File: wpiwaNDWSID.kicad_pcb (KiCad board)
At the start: 2 copper layers, 25 parts, among them J1 Conn_01x06, J2 Conn_01x03, J3 Conn_01x03, J4 Conn_01x03, J5 Conn_01x02, J6 Conn_01x03, U1 ESP32-S3-WROOM-1, U2 74AHCT125, U3 AP63205WU, U4 AP7363-33D-13

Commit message: final design
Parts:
- removed C5: 2200uF, Capacitor_THT:CP_Radial_D8.0mm_P3.80mm
- removed J3, J4, J6: Conn_01x03, Connector_Wire:SolderWire-1.5sqmm_1x03_P7.8mm_D1.7mm_OD3.9mm
- J2: value Conn_01x03 -> Conn_01x04; footprint Connector_Wire:SolderWire-1.5sqmm_1x03_P7.8mm_D1.7mm_OD3.9mm -> Connector_Wire:SolderWire-1.5sqmm_1x04_P7.8mm_D1.7mm_OD3.9mm
- J5: footprint Connector_Wire:SolderWire-2sqmm_1x02_P7.8mm_D2mm_OD3.9mm -> Connector_Wire:SolderWire-1.5sqmm_1x02_P7.8mm_D1.7mm_OD3.9mm
- moved J1 75.7 mm to (152.9, 123.4), turned to 180 degrees
- moved C2 55.2 mm to (143.4, 124.0), turned to 90 degrees
- moved U4 53.2 mm to (145.1, 113.2)
- moved C1 46.8 mm to (146.9, 121.1), turned to 180 degrees
- moved C3 46.0 mm to (161.8, 123.3)
- moved U1 45.4 mm to (165.8, 111.3)
- moved R1 44.8 mm to (159.3, 122.0), turned to 0 degrees
- moved C4 44.5 mm to (131.0, 114.4)
- moved U3 40.4 mm to (130.2, 118.5)
- moved C7 40.3 mm to (130.7, 122.5)
- moved C8 40.3 mm to (136.7, 115.5), turned to 90 degrees
- moved C9 37.5 mm to (136.7, 118.4), turned to -90 degrees
- moved L1 36.2 mm to (133.4, 121.0), turned to 90 degrees
- moved J2 35.4 mm to (200.0, 100.0), turned to -90 degrees
- moved C6 34.9 mm to (129.8, 110.2), turned to 0 degrees
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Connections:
- C3 pad 1: Net-(J1-Pin_5) -> Net-(J1-Pin_2)
- J1 pad 3: Net-(J1-Pin_3) -> +3.3V
- J1 pad 6: +3.3V -> Net-(J1-Pin_6)
- J2 pad 1: GND -> /LED Driver/LED1_OUT
- J2 pad 2: /LED Driver/LED1_OUT -> /LED Driver/LED2_OUT
- J2 pad 3: +12V -> /LED Driver/LED3_OUT
- R1 pad 2: Net-(J1-Pin_5) -> Net-(J1-Pin_2)
- U1 pad 18: /ESP32/LED_1 -> /ESP32/LED_4
- U1 pad 19: /ESP32/LED_2 -> /ESP32/LED_3
- U1 pad 20: /ESP32/LED_3 -> /ESP32/LED_2
- U1 pad 21: /ESP32/LED_4 -> /ESP32/LED_1
- U1 pad 27: Net-(J1-Pin_4) -> Net-(J1-Pin_6)
- U1 pad 3: Net-(J1-Pin_5) -> Net-(J1-Pin_2)
- U1 pad 36: Net-(J1-Pin_2) -> Net-(J1-Pin_4)
- U1 pad 37: Net-(J1-Pin_3) -> Net-(J1-Pin_5)
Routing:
- net GND: track 0.00 -> 55.2 mm, vias 0 -> 7
- net +5V: track 42.7 -> 91.1 mm
- net Net-(J1-Pin_6): track 0.00 -> 30.9 mm
- net Net-(J1-Pin_4): track 0.00 -> 17.2 mm
- net /ESP32/LED_1: track 0.00 -> 17.2 mm
- net Net-(R5-Pad1): track 0.00 -> 15.7 mm
- net /ESP32/LED_4: track 0.00 -> 15.0 mm
- net Net-(R4-Pad1): track 0.00 -> 14.5 mm
- net Net-(R2-Pad1): track 0.00 -> 13.4 mm
- net /ESP32/LED_2: track 0.00 -> 13.1 mm
- net Net-(R3-Pad1): track 0.00 -> 12.8 mm
- net Net-(J1-Pin_2): track 0.00 -> 12.7 mm
- net /ESP32/LED_3: track 0.00 -> 11.3 mm
- net Net-(J1-Pin_5): track 4.79 -> 14.1 mm
- net Net-(U3-SW): track 0.00 -> 7.46 mm
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- added copper zone on B.Cu, net GND
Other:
- board outline added: 78 x 30 mm
- board text added: "+12V"
- board text added: "GND"
- board text added: "KV0R - Nic DeBruin WPIWA NDWSID Controller October 2025"
- board text added: "Mounting Pattern 20x40mm, M3 or #6"
- board text added: "OUT1 Pin13"
- board text added: "OUT2 Pin12"
- board text added: "OUT3 Pin11"
- board text added: "OUT4 Pin10"

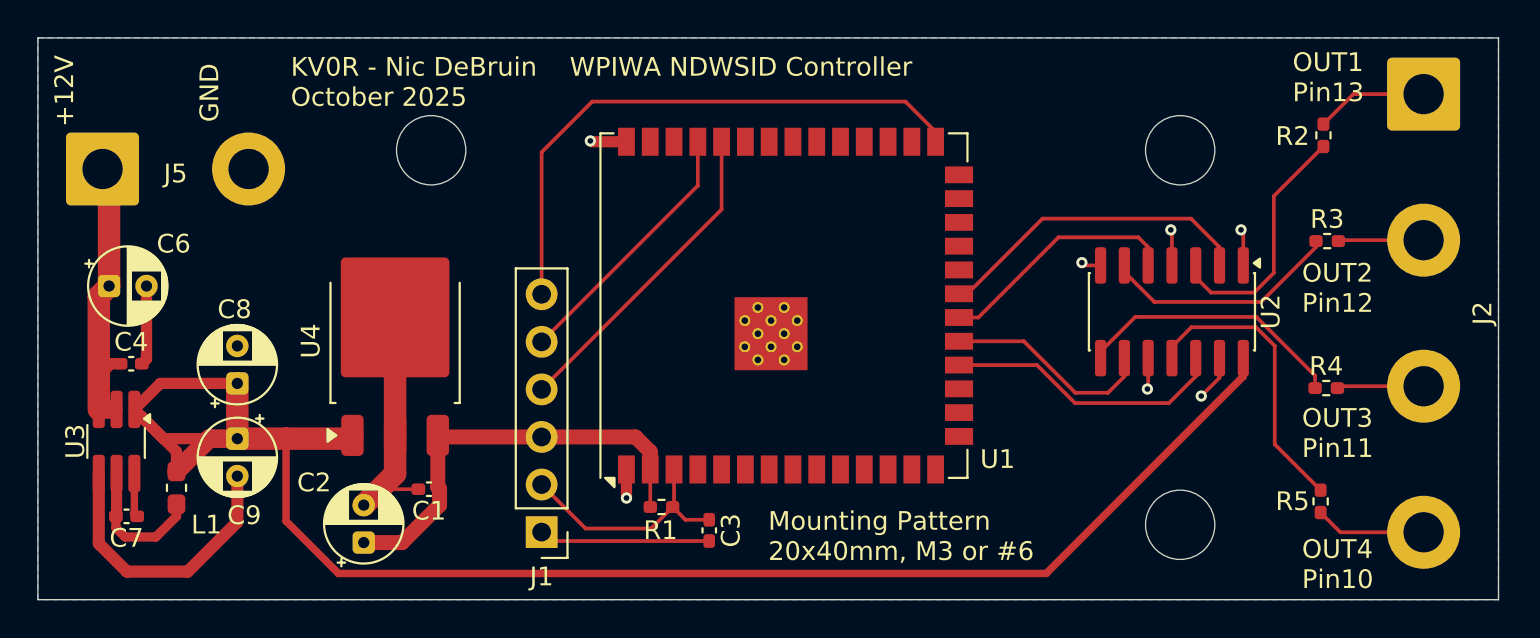
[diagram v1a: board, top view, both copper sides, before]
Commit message: all one layer added usb
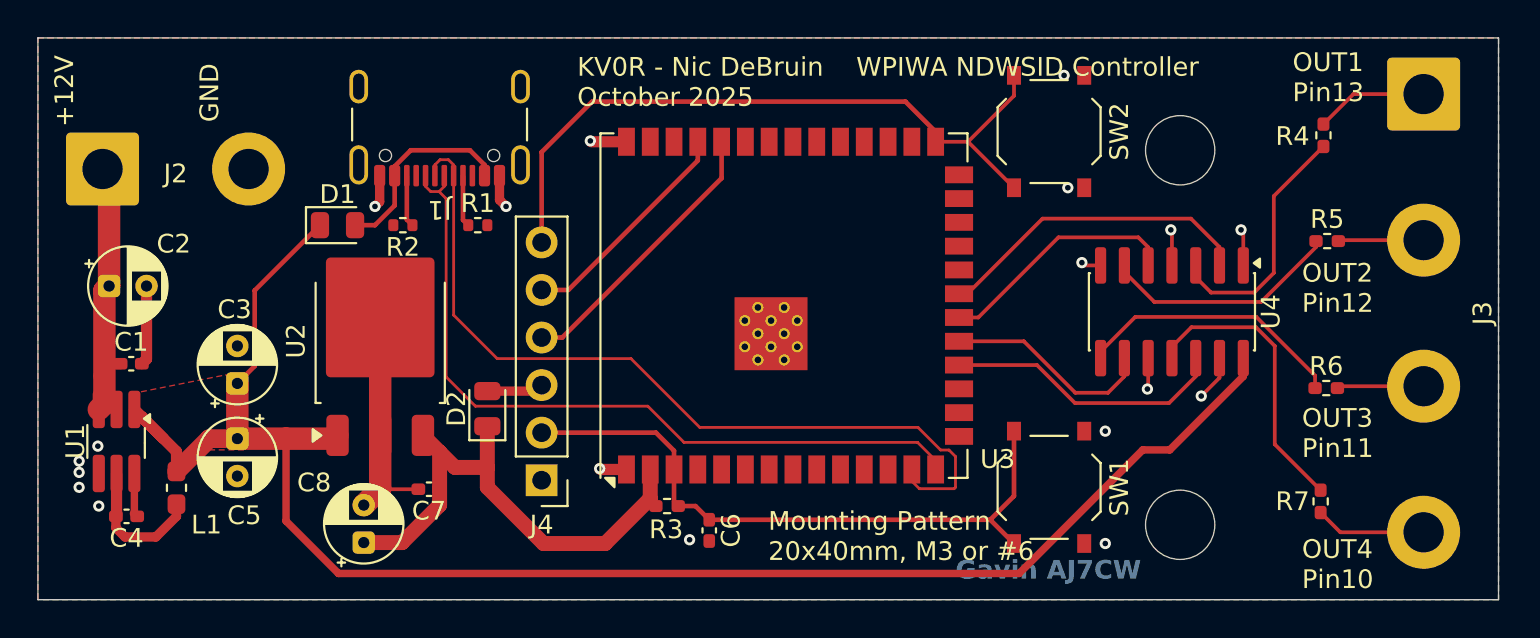
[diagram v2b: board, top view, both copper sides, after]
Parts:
- added D1: CTS05S30, Diode_SMD:D_0805_2012Metric, F.Cu at (142.0, 107.0)
- added D2: CTS05S30, Diode_SMD:D_0805_2012Metric, F.Cu at (150.0, 116.8)
- added J1: USB_C_Receptacle_USB2.0_16P, Connector_USB:USB_C_Receptacle_GCT_USB4105-xx-A_16P_TopMnt_Horizontal, F.Cu at (147.4, 100.7)
- added R1: 5.1K, Resistor_SMD:R_0402_1005Metric, F.Cu at (149.5, 107.0)
- added R2: 5.1K, Resistor_SMD:R_0402_1005Metric, F.Cu at (145.5, 107.0)
- added SW1: SW_Push, Button_Switch_SMD:SW_Push_1P1T_XKB_TS-1187A, F.Cu at (180.0, 121.0)
- added SW2: SW_Push, Button_Switch_SMD:SW_Push_1P1T_XKB_TS-1187A, F.Cu at (180.0, 102.0)
- moved J4 2.77 mm to (152.9, 120.6)
- moved U2 0.79 mm to (144.3, 113.2)
- moved R3 0.30 mm to (159.6, 122.0)
- renumbered C4 to C1, C6 to C2, C8 to C3, C7 to C4, C9 to C5, C3 to C6, C1 to C7, C2 to C8, J5 to J2, J2 to J3, J1 to J4, R1 to R3, R2 to R4, R3 to R5, R4 to R6, R5 to R7, U3 to U1, U4 to U2, U1 to U3, U2 to U4
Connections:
- J4 pad 3: +3.3V -> Net-(D2-A)
- U3 pad 13: unconnected-(U1-USB_D--Pad13) -> /ESP32/D-
- U3 pad 14: unconnected-(U1-USB_D+-Pad14) -> /ESP32/D+
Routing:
- net /ESP32/D-: track 0.00 -> 44.5 mm
- net /ESP32/D+: track 0.00 -> 40.9 mm
- net Net-(J4-Pin_2): track 12.7 -> 35.0 mm
- net GND: track 55.2 -> 34.2 mm, vias 7 -> 19
- net Net-(D1-A): track 0.00 -> 10.7 mm
- net Net-(J4-Pin_6): track 30.9 -> 37.9 mm
- net +3.3V: track 23.3 -> 29.6 mm
- net Net-(D2-A): track 0.00 -> 3.03 mm
- net Net-(J1-CC2): track 0.00 -> 2.77 mm
- net Net-(J1-CC1): track 0.00 -> 2.76 mm
- net +12V: track 17.2 -> 14.6 mm
- net Net-(J4-Pin_4): track 17.2 -> 15.1 mm
- net Net-(J4-Pin_5): track 14.1 -> 12.2 mm
- net +5V: track 91.1 -> 90.6 mm
- added copper zone on F.Cu, net +5V
- added copper zone on F.Cu, net GND
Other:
- outline, holes or cut-outs redrawn
- board text added: "Gavin AJ7CW"

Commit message: final commit
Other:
- board size 78 x 30 mm -> 85.8 x 30 mm
- board text added: "Mounting Pattern 65x20mm, M3 or #6"
- board text added: "Nic KV0R Gavin AJ7CW"
- board text added: "WPIWA NDWSID Controller"
- board text removed: "Gavin AJ7CW"
- board text removed: "KV0R - Nic DeBruin WPIWA NDWSID Controller October 2025"
- board text removed: "Mounting Pattern 20x40mm, M3 or #6"
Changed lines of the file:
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@@
 		(tags "2.4 GHz Wi-Fi and Bluetooth module")
 		(property "Reference" "U3"
-			(at -8.204394 11.41 0)
+			(at -10.704394 5.16 0)
 			(unlocked yes)
 			(layer "F.SilkS")
@@
 		(tags "diode")
 		(property "Reference" "D2"
-			(at 0 -1.65 90)
+			(at 2.8 0 90)
 			(layer "F.SilkS")
 			(effects
@@
 	)
 	(gr_rect
-		(start 147 103)
+		(start 122 103)
 		(end 187 123)
 		(stroke
@@
 		(layer "Edge.Cuts")
 	)
+	(gr_circle
+		(center 122 123)
+		(end 123.85 123)
+		(stroke
+			(width 0.05)
+			(type solid)
+		)
+		(fill no)
+		(layer "Edge.Cuts")
+	)
+	(gr_circle
+		(center 122 103)
+		(end 123.85 103)
+		(stroke
+			(width 0.05)
+			(type solid)
+		)
+		(fill no)
+		(layer "Edge.Cuts")
+	)
 	(gr_rect
-		(start 126 97)
+		(start 118.2 97)
 		(end 204 127)
 		(stroke
@@
 		(layer "Edge.Cuts")
 	)
-	(gr_text "Gavin AJ7CW"
-		(at 175 126 0)
-		(layer "B.Cu" knockout)
+	(gr_text "Nic KV0R\nGavin AJ7CW"
+		(at 123 107.6 270)
+		(layer "F.Cu" knockout)
 		(effects
 			(font
@@
 		)
 	)
-	(gr_text "KV0R - Nic DeBruin	WPIWA NDWSID Controller\nOctober 2025"
-		(at 154.8 100.75 0)
+	(gr_text "WPIWA NDWSID Controller\n"
+		(at 155.4 99.6 0)
 		(layer "F.SilkS")
 		(effects
@@
 		)
 	)
-	(gr_text "Mounting Pattern\n20x40mm, M3 or #6\n"
-		(at 165 125 0)
+	(gr_text "Mounting Pattern\n65x20mm, M3 or #6\n"
+		(at 119.4 105.4 270)
 		(layer "F.SilkS")
 		(effects
@@
 		(polygon
 			(pts
-				(xy 126 97) (xy 204 97) (xy 204 127) (xy 126 127)
+				(xy 118.2 97) (xy 204 97) (xy 204 127) (xy 118.2 127)
 			)
 		)

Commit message: rev 2
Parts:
- removed C2: 10uF, Capacitor_THT:CP_Radial_D4.0mm_P2.00mm
- removed C3, C5: 22uF, Capacitor_THT:CP_Radial_D4.0mm_P2.00mm
- removed C4: 0.1uF, Capacitor_SMD:C_0402_1005Metric_Pad0.74x0.62mm_HandSolder
- removed L1: 4.7uH, Inductor_SMD:L_0603_1608Metric_Pad1.05x0.95mm_HandSolder
- removed U1: AP63205WU, Package_TO_SOT_SMD:TSOT-23-6_HandSoldering
- C1: value 0.1uF -> 22uF; footprint Capacitor_SMD:C_0402_1005Metric_Pad0.74x0.62mm_HandSolder -> Capacitor_THT:CP_Radial_D4.0mm_P2.00mm
- C6, C7: footprint Capacitor_SMD:C_0402_1005Metric_Pad0.74x0.62mm_HandSolder -> Capacitor_SMD:C_0402_1005Metric
- D1, D2: footprint Diode_SMD:D_0805_2012Metric -> Diode_SMD:D_0402_1005Metric_Pad0.77x0.64mm_HandSolder
- J2: footprint Connector_Wire:SolderWire-1.5sqmm_1x02_P7.8mm_D1.7mm_OD3.9mm -> Connector_Wire:SolderWire-0.75sqmm_1x02_P4.8mm_D1.25mm_OD2.3mm
- J3: footprint Connector_Wire:SolderWire-1.5sqmm_1x04_P7.8mm_D1.7mm_OD3.9mm -> Connector_Wire:SolderWire-0.75sqmm_1x04_P4.8mm_D1.25mm_OD2.3mm
- J4: value Conn_01x06 -> Conn_01x03; footprint Connector_PinHeader_2.54mm:PinHeader_1x06_P2.54mm_Vertical -> Connector_Wire:SolderWire-0.75sqmm_1x03_P4.8mm_D1.25mm_OD2.3mm
- moved C1 52.1 mm to (180.1, 97.1), turned to -90 degrees
- moved C8 49.8 mm to (185.3, 97.1), turned to -90 degrees
- moved U2 46.9 mm to (183.3, 87.0)
- moved J2 46.5 mm to (175.9, 101.8), turned to 180 degrees
- moved C7 46.2 mm to (184.8, 94.6)
- moved J4 45.5 mm to (195.6, 104.8), turned to 0 degrees
- moved SW2 38.5 mm to (214.8, 85.5), turned to 180 degrees
- moved U3 37.4 mm to (197.9, 92.1)
- moved R3 37.2 mm to (191.5, 102.8)
- moved C6 35.2 mm to (191.5, 104.4), turned to 180 degrees
- moved U4 32.3 mm to (215.1, 96.5)
- moved D1 32.1 mm to (172.7, 97.5), turned to 180 degrees
- moved D2 31.9 mm to (176.0, 98.2), turned to -90 degrees
- moved R2 30.3 mm to (173.4, 95.0), turned to 0 degrees
- moved R5 29.2 mm to (218.9, 91.3)
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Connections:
- C1 pad 1: +12V -> +5V
- C6 pad 1: Net-(J4-Pin_2) -> Net-(U3-EN)
- D2 pad 1: +3.3V -> +5V
- J2 pad 1: +12V -> Net-(D2-A)
- J4 pad 1: GND -> +3.3V
- J4 pad 2: Net-(J4-Pin_2) -> /ESP32/RELAY
- J4 pad 3: Net-(D2-A) -> GND
- R3 pad 2: Net-(J4-Pin_2) -> Net-(U3-EN)
- SW1 pad 2: Net-(J4-Pin_2) -> Net-(U3-EN)
- SW2 pad 2: Net-(J4-Pin_6) -> Net-(U3-IO0)
- U3 pad 26: unconnected-(U3-IO45-Pad26) -> GND
- U3 pad 27: Net-(J4-Pin_6) -> Net-(U3-IO0)
- U3 pad 3: Net-(J4-Pin_2) -> Net-(U3-EN)
- U3 pad 36: Net-(J4-Pin_4) -> unconnected-(U3-RXD0-Pad36)
- U3 pad 37: Net-(J4-Pin_5) -> unconnected-(U3-TXD0-Pad37)
- U3 pad 9: unconnected-(U3-IO16-Pad9) -> /ESP32/RELAY
- U4 pad 11: Net-(R7-Pad1) -> Net-(R6-Pad1)
- U4 pad 12: /ESP32/LED_4 -> /ESP32/LED_3
- U4 pad 2: /ESP32/LED_1 -> /ESP32/LED_2
- U4 pad 3: Net-(R4-Pad1) -> Net-(R5-Pad1)
- U4 pad 5: /ESP32/LED_2 -> /ESP32/LED_1
- U4 pad 6: Net-(R5-Pad1) -> Net-(R4-Pad1)
- U4 pad 8: Net-(R6-Pad1) -> Net-(R7-Pad1)
- U4 pad 9: /ESP32/LED_3 -> /ESP32/LED_4
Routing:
- net Net-(J4-Pin_6): track 37.9 -> 0.00 mm
- net +5V: track 90.6 -> 53.7 mm, vias 0 -> 1
- net Net-(J4-Pin_2): track 35.0 -> 0.00 mm
- net GND: track 34.2 -> 0.00 mm, vias 19 -> 8
- net Net-(U3-EN): track 0.00 -> 16.5 mm
- net Net-(J4-Pin_4): track 15.1 -> 0.00 mm
- net +12V: track 14.6 -> 0.00 mm
- net Net-(J4-Pin_5): track 12.2 -> 0.00 mm
- net Net-(R7-Pad1): track 15.7 -> 3.62 mm
- net Net-(U3-IO0): track 0.00 -> 12.0 mm
- net Net-(R6-Pad1): track 14.5 -> 3.94 mm
- net Net-(R4-Pad1): track 13.4 -> 3.30 mm
- net Net-(R5-Pad1): track 12.8 -> 3.52 mm
- net /ESP32/LED_1: track 17.2 -> 9.68 mm
- net Net-(U1-SW): track 7.46 -> 0.00 mm
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- removed copper zone on F.Cu, net +5V
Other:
- board size 85.8 x 30 mm -> 71.4 x 26.2 mm
- board text removed: "+12V"
- board text removed: "GND"
- board text removed: "Mounting Pattern 65x20mm, M3 or #6"
- board text removed: "Nic KV0R Gavin AJ7CW"
- board text removed: "OUT1 Pin13"
- board text removed: "OUT2 Pin12"
- board text removed: "OUT3 Pin11"
- board text removed: "OUT4 Pin10"
- board text removed: "WPIWA NDWSID Controller"
